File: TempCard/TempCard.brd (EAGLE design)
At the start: 100 x 80 mm, 26 parts, among them Q1 MOSFET-NCHANNELBSS138, Q2 MOSFET-NCHANNELBSS138, Q3 MOSFET-NCHANNELBSS138, Q4 MOSFET-NCHANNELBSS138, U1 MIC5219 3.3V

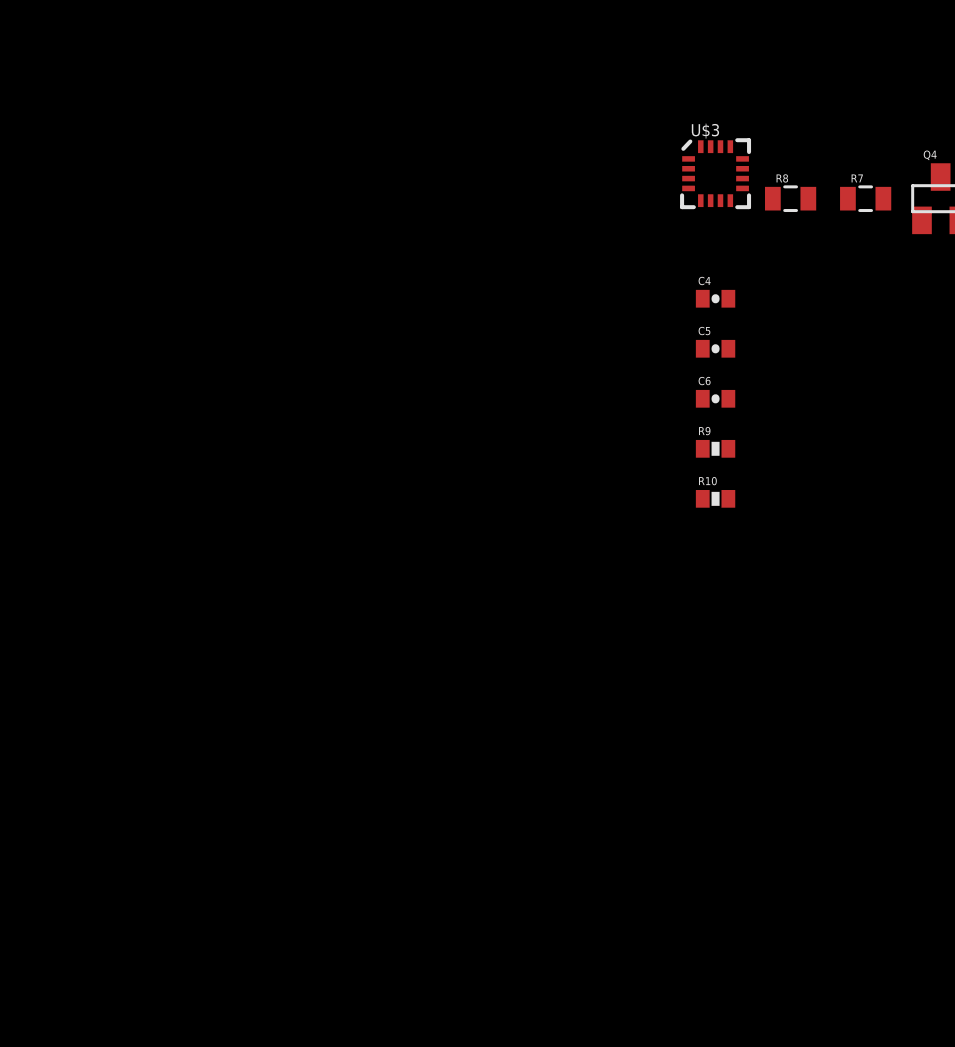
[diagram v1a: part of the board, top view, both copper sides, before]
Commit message: MCU/Sensor Edit
Switched the magnetometer. Added potential MCUs for Atmel and PIC. More than likely going with ATTiny85. More testing to follow.

Signed-off-by: Scott Lerner <scottphiliplerner@gmail.com>
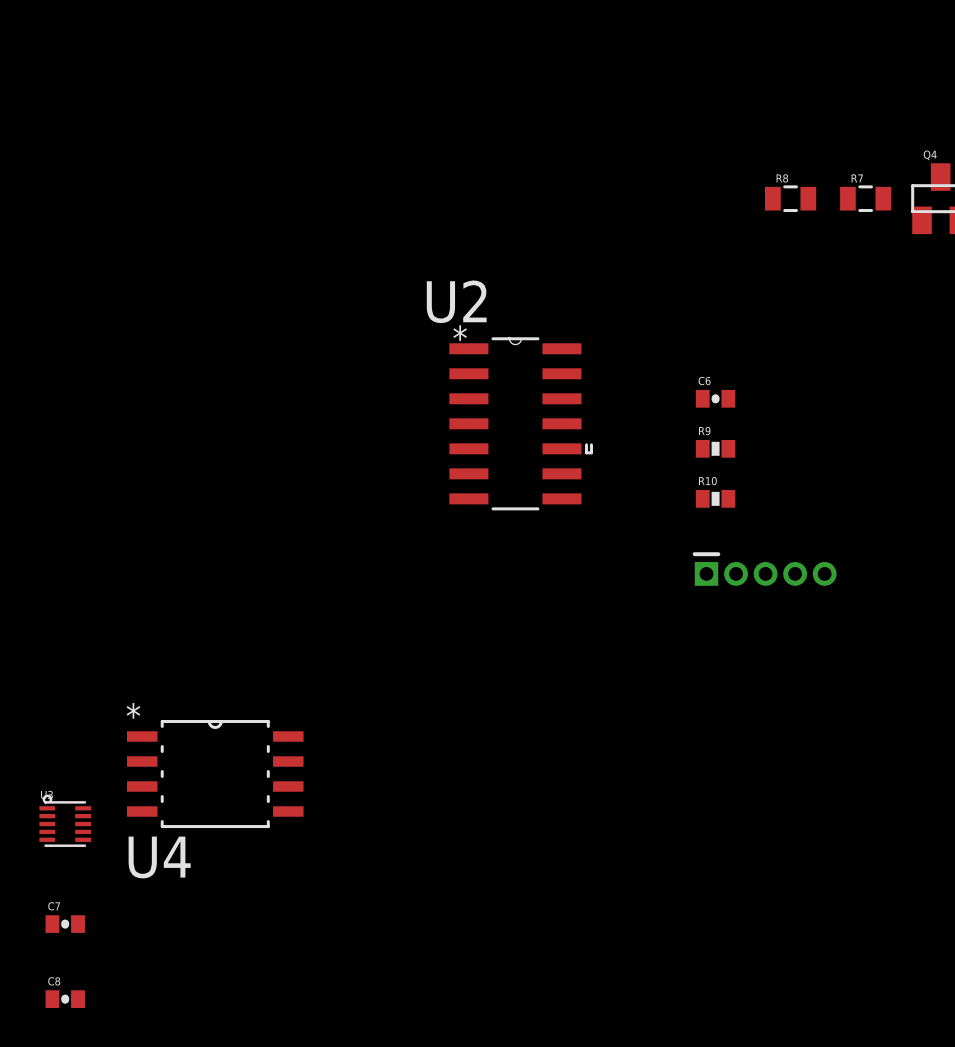
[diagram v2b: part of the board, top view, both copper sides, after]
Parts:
- removed C4: 4.7uF, SparkFun-Passives:0402-CAP
- removed C5: 0.22uF, SparkFun-Passives:0402-CAP
- removed U$3: HMC5883LSMD, SparkFun-Sensors:16LPCC
- added C7, C8: 0.1uF, SparkFun-Passives:0402-CAP
- added U$4: PIC-ICSP-MINI, SparkFun-Connectors:PIC-ICSP-MINI
- added U2: PIC16F688-I/SL, Microchip_By_element14_Batch_1:SOIC127P600X175-14N
- added U3: MAG3110, SparkFun-Sensors:DFN-10
- added U4: ATTINY85-20SU, Atmel_By_element14_Batch_1:SOIC127P798X216-8N
- R10, R9: value DNP -> 10k
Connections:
- removed net N$10: R9.1, U$3.1
- removed net N$11: R10.1, U$3.16
- removed net N$3: C4.1, U$3.10
- removed net N$7: C5.1, U$3.8
- removed net N$8: C5.2, U$3.12
- new net INT1: U3.9
- new net N$12: C7.1, U3.1
- new net N$13: C8.1, U3.4
- new net SCL: R10.1, U3.7
- new net SDA: R9.1, U3.6
- new net VCC: U4.8
- new net VDD: U2.1
- net 3.3V: now also U3.2, U3.8; no longer U$3.13, U$3.2, U$3.4
- net GND: now also C7.2, C8.2, U3.10, U3.5; no longer C4.2, U$3.11, U$3.9
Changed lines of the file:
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@@
 <element name="R7" library="SparkFun-Resistors" package="0805" value="" x="-68.58" y="-16.51"/>
 <element name="R8" library="SparkFun-Resistors" package="0805" value="" x="-72.39" y="-16.51"/>
-<element name="U$3" library="SparkFun-Sensors" package="16LPCC" value="HMC5883LSMD" x="-76.2" y="-15.24"/>
-<element name="C4" library="SparkFun-Passives" package="0402-CAP" value="4.7uF" x="-76.2" y="-21.59"/>
-<element name="C5" library="SparkFun-Passives" package="0402-CAP" value="0.22uF" x="-76.2" y="-24.13"/>
 <element name="C6" library="SparkFun-Passives" package="0402-CAP" value="0.1uF" x="-76.2" y="-26.67"/>
-<element name="R9" library="SparkFun-Passives" package="0402-RES" value="DNP" x="-76.2" y="-29.21"/>
-<element name="R10" library="SparkFun-Passives" package="0402-RES" value="DNP" x="-76.2" y="-31.75"/>
+<element name="R9" library="SparkFun-Passives" package="0402-RES" value="10k" x="-76.2" y="-29.21"/>
+<element name="R10" library="SparkFun-Passives" package="0402-RES" value="10k" x="-76.2" y="-31.75"/>
+<element name="U$4" library="SparkFun-Connectors" package="PIC-ICSP-MINI" value="PIC-ICSP-MINI" x="-73.66" y="-35.56"/>
+<element name="U2" library="Microchip_By_element14_Batch_1" package="SOIC127P600X175-14N" value="PIC16F688-I/SL" x="-86.36" y="-27.94">
+<attribute name="PACKAGE" value="14SOIC" x="-86.36" y="-27.94" size="1.778" layer="27" ratio="15" display="off"/>
+<attribute name="OC_NEWARK" value="89H0500" x="-86.36" y="-27.94" size="1.778" layer="27" ratio="15" display="off"/>
+<attribute name="MPN" value="PIC16F688-I/SL" x="-86.36" y="-27.94" size="1.778" layer="27" ratio="15" display="off"/>
+<attribute name="SUPPLIER" value="Microchip Technology" x="-86.36" y="-27.94" size="1.778" layer="27" ratio="15" display="off"/>
+<attribute name="OC_FARNELL" value="9760571" x="-86.36" y="-27.94" size="1.778" layer="27" ratio="15" display="off"/>
+</element>
+<element name="U4" library="Atmel_By_element14_Batch_1" package="SOIC127P798X216-8N" value="ATTINY85-20SU" x="-101.6" y="-45.72">
+<attribute name="PACKAGE" value="SOIC-8" x="-101.6" y="-45.72" size="1.778" layer="27" ratio="15" display="off"/>
+<attribute name="OC_NEWARK" value="58M3797" x="-101.6" y="-45.72" size="1.778" layer="27" ratio="15" display="off"/>
+<attribute name="MPN" value="ATTINY85-20SU" x="-101.6" y="-45.72" size="1.778" layer="27" ratio="15" display="off"/>
+<attribute name="SUPPLIER" value="Atmel" x="-101.6" y="-45.72" size="1.778" layer="27" ratio="15" display="off"/>
+<attribute name="OC_FARNELL" value="1455164" x="-101.6" y="-45.72" size="1.778" layer="27" ratio="15" display="off"/>
+</element>
+<element name="U3" library="SparkFun-Sensors" package="DFN-10" value="MAG3110" x="-109.22" y="-48.26"/>
+<element name="C7" library="SparkFun-Passives" package="0402-CAP" value="0.1uF" x="-109.22" y="-53.34"/>
+<element name="C8" library="SparkFun-Passives" package="0402-CAP" value="0.1uF" x="-109.22" y="-57.15"/>
 </elements>
 <signals>
@@
 <contactref element="U$2" pad="1"/>
 <contactref element="C3" pad="2"/>
-<contactref element="C4" pad="2"/>
-<contactref element="U$3" pad="9"/>
-<contactref element="U$3" pad="11"/>
 <contactref element="C6" pad="2"/>
-<wire x1="-75.55" y1="-21.59" x2="-75.55" y2="-26.67" width="0" layer="19" extent="1-1"/>
-<wire x1="-74.83" y1="-15.99" x2="-75.55" y2="-21.59" width="0" layer="19" extent="1-1"/>
-<wire x1="-74.83" y1="-14.99" x2="-74.83" y2="-15.99" width="0" layer="19" extent="1-1"/>
-<wire x1="-48.63" y1="-16.51" x2="-74.83" y2="-15.99" width="0" layer="19" extent="1-1"/>
+<contactref element="C7" pad="2"/>
+<contactref element="C8" pad="2"/>
+<contactref element="U3" pad="5"/>
+<contactref element="U3" pad="10"/>
+<wire x1="-108.57" y1="-53.34" x2="-108.57" y2="-57.15" width="0" layer="19" extent="1-1"/>
+<wire x1="-110.13" y1="-49.06" x2="-108.57" y2="-53.34" width="0" layer="19" extent="1-1"/>
+<wire x1="-108.31" y1="-47.46" x2="-110.13" y2="-49.06" width="0" layer="19" extent="1-1"/>
+<wire x1="-75.55" y1="-26.67" x2="-108.31" y2="-47.46" width="0" layer="19" extent="1-1"/>
+<wire x1="-48.63" y1="-16.51" x2="-75.55" y2="-26.67" width="0" layer="19" extent="1-1"/>
 <wire x1="-29.58" y1="-16.51" x2="-48.63" y2="-16.51" width="0" layer="19" extent="1-1"/>
 <wire x1="-26.67" y1="-17.8101" x2="-29.58" y2="-16.51" width="0" layer="19" extent="1-1"/>
@@
 <contactref element="U$2" pad="4"/>
 <contactref element="C3" pad="1"/>
-<contactref element="U$3" pad="4"/>
-<contactref element="U$3" pad="13"/>
-<contactref element="U$3" pad="2"/>
 <contactref element="R9" pad="2"/>
 <contactref element="R10" pad="2"/>
 <contactref element="C6" pad="1"/>
+<contactref element="U3" pad="2"/>
+<contactref element="U3" pad="8"/>
+<wire x1="-108.31" y1="-48.26" x2="-110.13" y2="-47.86" width="0" layer="19" extent="1-1"/>
+<wire x1="-75.55" y1="-31.75" x2="-108.31" y2="-48.26" width="0" layer="19" extent="1-1"/>
 <wire x1="-75.55" y1="-29.21" x2="-75.55" y2="-31.75" width="0" layer="19" extent="1-1"/>
 <wire x1="-76.85" y1="-26.67" x2="-75.55" y2="-29.21" width="0" layer="19" extent="1-1"/>
-<wire x1="-77.57" y1="-15.99" x2="-76.85" y2="-26.67" width="0" layer="19" extent="1-1"/>
-<wire x1="-77.57" y1="-14.99" x2="-77.57" y2="-15.99" width="0" layer="19" extent="1-1"/>
-<wire x1="-75.45" y1="-13.87" x2="-77.57" y2="-14.99" width="0" layer="19" extent="1-1"/>
-<wire x1="-67.68" y1="-16.51" x2="-75.45" y2="-13.87" width="0" layer="19" extent="1-1"/>
+<wire x1="-67.68" y1="-16.51" x2="-76.85" y2="-26.67" width="0" layer="19" extent="1-1"/>
 <wire x1="-65.72" y1="-17.61" x2="-67.68" y2="-16.51" width="0" layer="19" extent="1-1"/>
 <wire x1="-58.1" y1="-17.61" x2="-65.72" y2="-17.61" width="0" layer="19" extent="1-1"/>
@@
 <wire x1="-11.557" y1="-14.605" x2="-54.24" y2="-16.51" width="0" layer="19" extent="1-1"/>
 </signal>
-<signal name="N$3">
-<contactref element="U$3" pad="10"/>
-<contactref element="C4" pad="1"/>
-<wire x1="-74.83" y1="-15.49" x2="-76.85" y2="-21.59" width="0" layer="19" extent="1-1"/>
+<signal name="VDD">
+<contactref element="U2" pad="1"/>
 </signal>
-<signal name="N$7">
-<contactref element="U$3" pad="8"/>
-<contactref element="C5" pad="1"/>
-<wire x1="-75.45" y1="-16.61" x2="-76.85" y2="-24.13" width="0" layer="19" extent="1-1"/>
+<signal name="VCC">
+<contactref element="U4" pad="8"/>
 </signal>
-<signal name="N$8">
-<contactref element="U$3" pad="12"/>
-<contactref element="C5" pad="2"/>
-<wire x1="-74.83" y1="-14.49" x2="-75.55" y2="-24.13" width="0" layer="19" extent="1-1"/>
+<signal name="N$12">
+<contactref element="U3" pad="1"/>
+<contactref element="C7" pad="1"/>
+<wire x1="-110.13" y1="-47.46" x2="-109.87" y2="-53.34" width="0" layer="19" extent="1-1"/>
 </signal>
-<signal name="N$11">
-<contactref element="U$3" pad="16"/>
+<signal name="N$13">
+<contactref element="U3" pad="4"/>
+<contactref element="C8" pad="1"/>
+<wire x1="-110.13" y1="-48.66" x2="-109.87" y2="-57.15" width="0" layer="19" extent="1-1"/>
+</signal>
+<signal name="INT1">
+<contactref element="U3" pad="9"/>
+</signal>
+<signal name="SDA">
+<contactref element="U3" pad="6"/>
+<contactref element="R9" pad="1"/>
+<wire x1="-76.85" y1="-29.21" x2="-108.31" y2="-49.06" width="0" layer="19" extent="1-1"/>
+</signal>
+<signal name="SCL">
+<contactref element="U3" pad="7"/>
 <contactref element="R10" pad="1"/>
-<wire x1="-76.95" y1="-13.87" x2="-76.85" y2="-31.75" width="0" layer="19" extent="1-1"/>
-</signal>
-<signal name="N$10">
-<contactref element="U$3" pad="1"/>
-<contactref element="R9" pad="1"/>
-<wire x1="-77.57" y1="-14.49" x2="-76.85" y2="-29.21" width="0" layer="19" extent="1-1"/>
+<wire x1="-76.85" y1="-31.75" x2="-108.31" y2="-48.66" width="0" layer="19" extent="1-1"/>
 </signal>
 </signals>

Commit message: Plane Stuff
I don't know what exactly this changed.

Signed-off-by: Scott Lerner <scottphiliplerner@gmail.com>
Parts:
- removed R10, R9: 10k, SparkFun-Passives:0402-RES
- removed U$4: PIC-ICSP-MINI, SparkFun-Connectors:PIC-ICSP-MINI
- removed U2: PIC16F688-I/SL, Microchip_By_element14_Batch_1:SOIC127P600X175-14N
- added C4: 0.1uF, SparkFun-Capacitors:0805
- added R11, R12: 10k, SparkFun-Resistors:0805
- moved U3 167.8 mm to (36.8, 34.3)
- moved C8 167.7 mm to (30.5, 35.6)
- moved C7 167.0 mm to (30.5, 38.1)
- moved U4 154.9 mm to (21.6, 48.3)
- moved R8 137.0 mm to (47.0, 50.8), turned to 90 degrees
- moved C6 133.6 mm to (40.6, 38.1)
- moved R6 130.0 mm to (47.0, 55.9), turned to 90 degrees
- moved R7 129.4 mm to (41.9, 50.8), turned to 90 degrees
- moved Q4 127.6 mm to (44.5, 49.5)
- moved Q3 124.0 mm to (44.5, 54.6)
- moved R5 119.6 mm to (41.9, 55.9), turned to 270 degrees
- moved R4 108.9 mm to (47.0, 40.6), turned to 90 degrees
- moved C3 107.2 mm to (31.8, 53.3), turned to 90 degrees
- moved R2 102.4 mm to (47.0, 45.7), turned to 90 degrees
- moved R3 101.4 mm to (41.9, 40.6), turned to 90 degrees
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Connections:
- removed net N$4: Q3.3, R6.1
- removed net N$6: Q4.3, R8.1
- removed net SCL_5V: Q2.3, R4.1
- removed net SDA_5V: Q1.3, R2.1
- removed net VCC: U4.8
- removed net VDD: U2.1
- net 3.3V: no longer R10.2, R9.2
- net 5V: now also C4.1, R11.2, R12.2, U4.8
- net GND: now also C4.2, U4.4
- net SCL: now also Q2.3, Q4.3, R12.1, R4.1, R8.1, U4.6; no longer R10.1
- net SDA: now also Q1.3, Q3.3, R11.1, R2.1, R6.1, U4.5; no longer R9.1

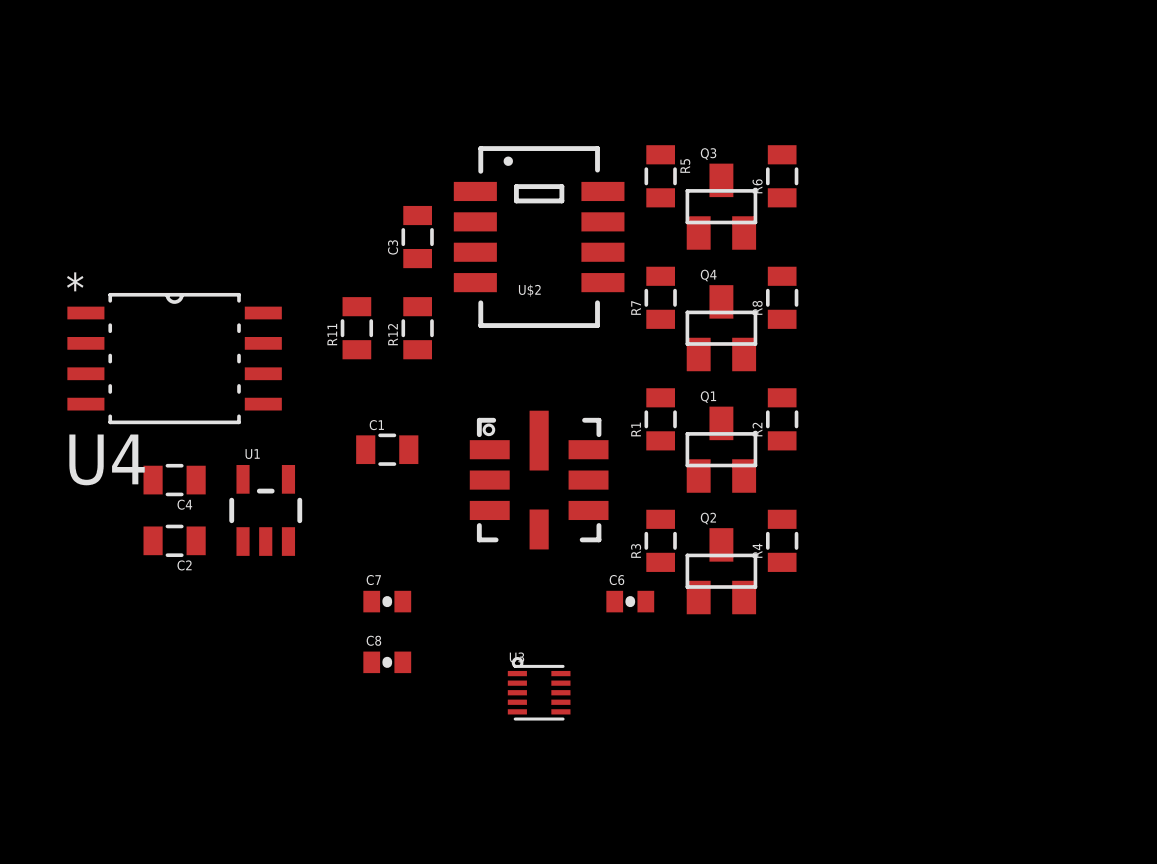
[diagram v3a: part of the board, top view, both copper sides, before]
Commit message: Final Hardware Selected
HTU21D, MAG3110, BMP180. Still room in the future for adding LCD screen as well as other functionality in different series.

Signed-off-by: Scott Lerner <scottphiliplerner@gmail.com>
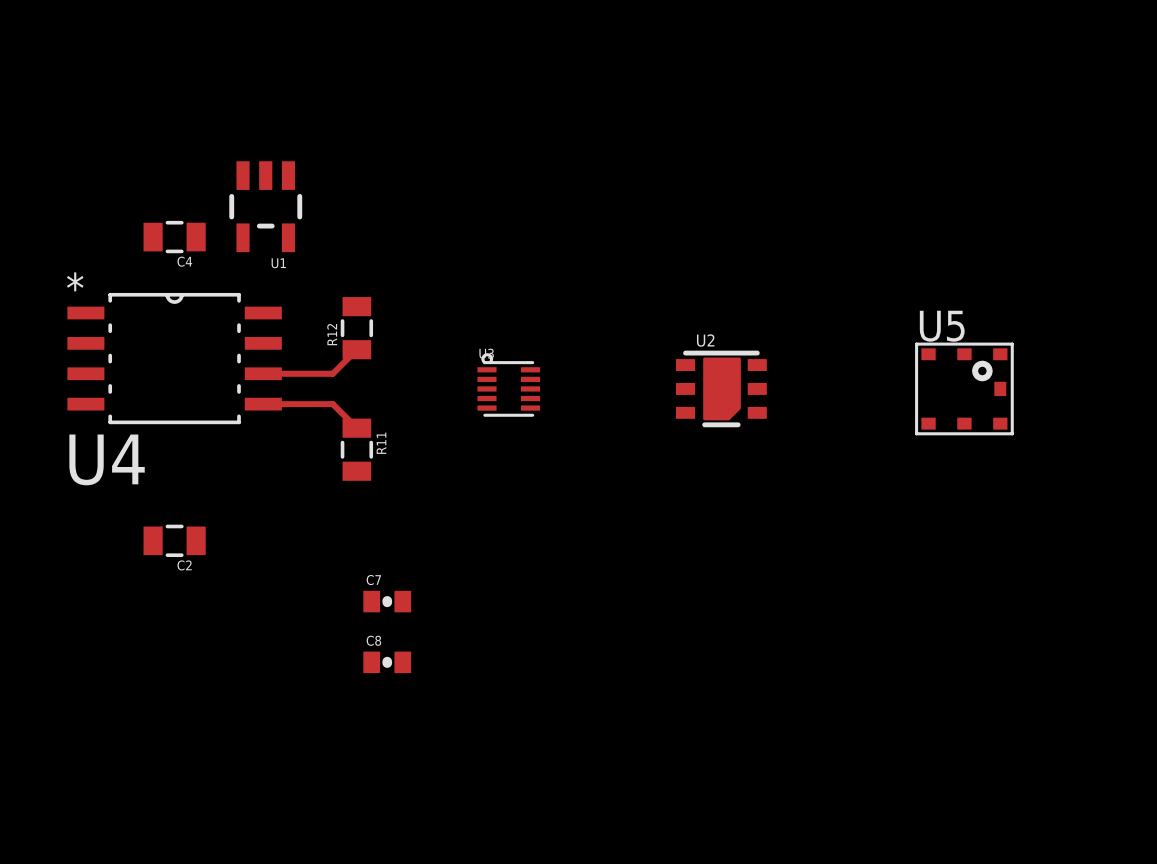
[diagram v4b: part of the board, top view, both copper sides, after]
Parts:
- removed C1: 1.0uF, SparkFun-Capacitors:0805
- removed C3: 0.1uF, SparkFun-Capacitors:0805
- removed C6: 0.1uF, SparkFun-Passives:0402-CAP
- removed Q1, Q2, Q3, Q4: MOSFET-NCHANNELBSS138, SparkFun-DiscreteSemi:SOT23
- removed R1, R2, R3, R4, R5, R6, R7, R8: (no value), SparkFun-Resistors:0805
- removed U$1: BMP085, SparkFun-Sensors:BMP085
- removed U$2: SHT1XSMD, SparkFun-Sensors:SHT1X
- added U2: HTU21DSMD, SparkFun-Sensors:HTU21D
- added U5: BMP180, SparkFun-Sensors:BMP180
- moved U3 12.8 mm to (35.6, 47.0)
- moved U1 12.7 mm to (25.4, 54.6), turned to 180 degrees
- moved C4 10.2 mm to (21.6, 53.3)
- moved R11 5.08 mm to (29.2, 44.5), turned to 270 degrees
- moved R12 2.54 mm to (29.2, 49.5)
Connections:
- removed net N$1: Q1.2, R1.1, U$1.7
- removed net N$2: Q2.2, R3.1, U$1.6
- removed net N$5: Q4.2, R7.1, U$2.3
- removed net N$9: Q3.2, R5.1, U$2.2
- net 3.3V: now also C4.1, R11.2, R12.2, U2.VDD, U4.8, U5.2, U5.3; no longer C1.1, C3.1, C6.1, Q1.1, Q2.1, Q3.1, Q4.1, R1.2, R3.2, R5.2, R7.2, U$1.3, U$1.4, U$2.4
- net 5V: no longer C4.1, R11.2, R12.2, R2.2, R4.2, R6.2, R8.2, U4.8
- net GND: now also U2.7, U2.GND, U5.7; no longer C1.2, C3.2, C6.2, U$1.1, U$2.1
- net SCL: no longer Q2.3, Q4.3, R4.1, R8.1
- net SDA: no longer Q1.3, Q3.3, R2.1, R6.1
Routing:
- net SCL: track 0.00 -> 4.33 mm
- net SDA: track 0.00 -> 4.33 mm
